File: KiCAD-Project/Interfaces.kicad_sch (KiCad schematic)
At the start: 56 parts, among them J201 XT30, J202 Conn_02x04_Odd_Even, J203 Conn_01x03_Shielded, J204 Conn_01x03_Shielded, U201 TI_TCAN337G, U202 TLE5012B_E1000, U203 MAX15062A

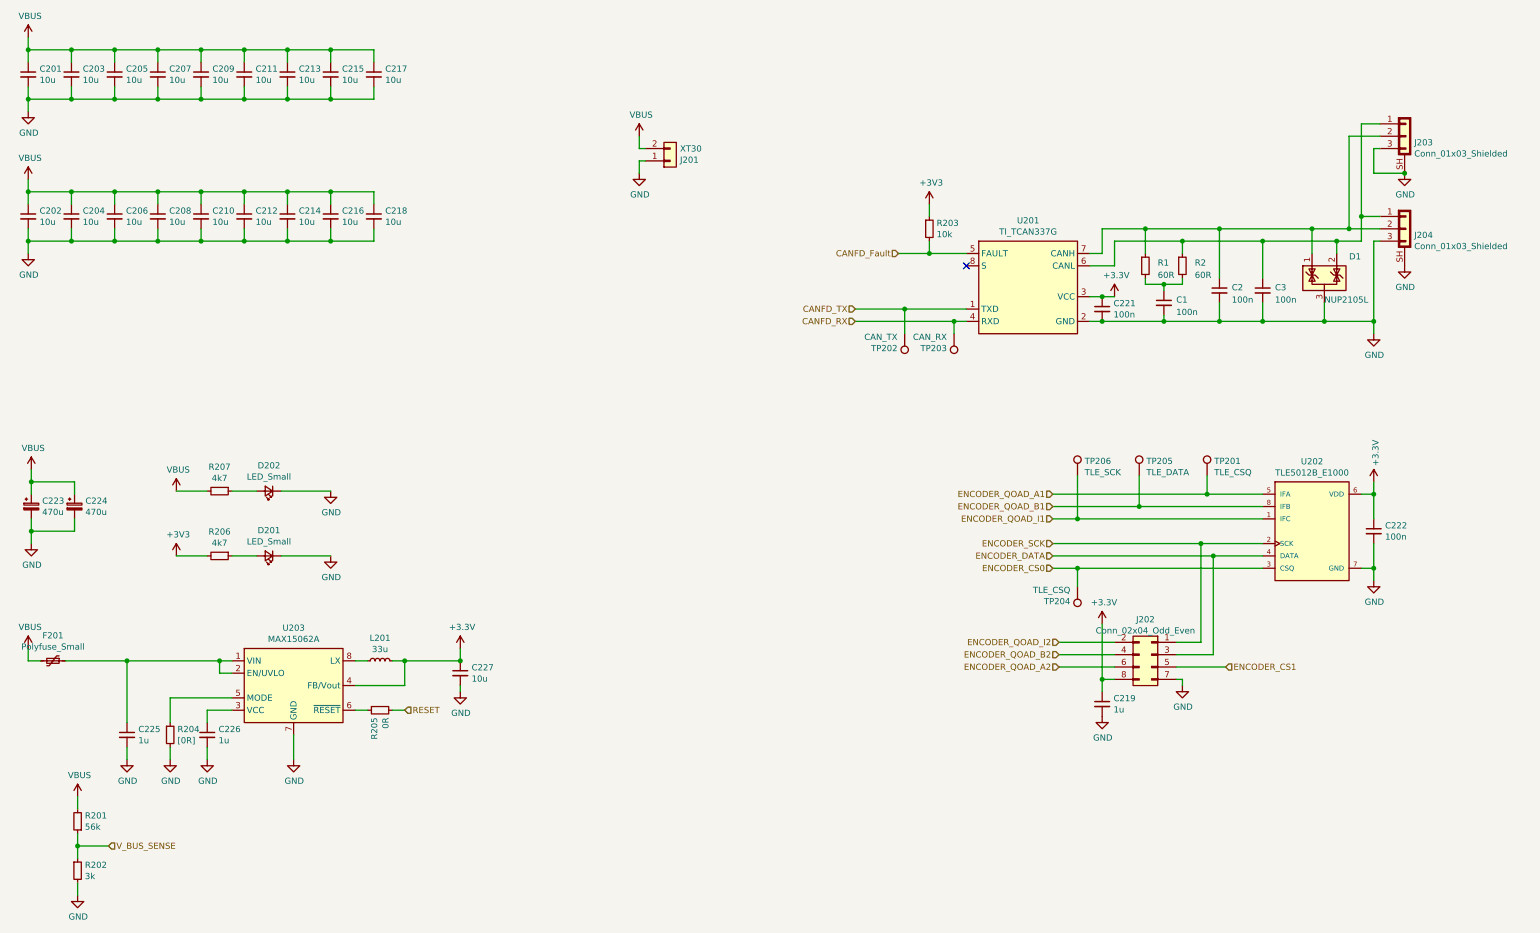
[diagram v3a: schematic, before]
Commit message: changed connectors to THT
changed connectors to THT, removed UART connector
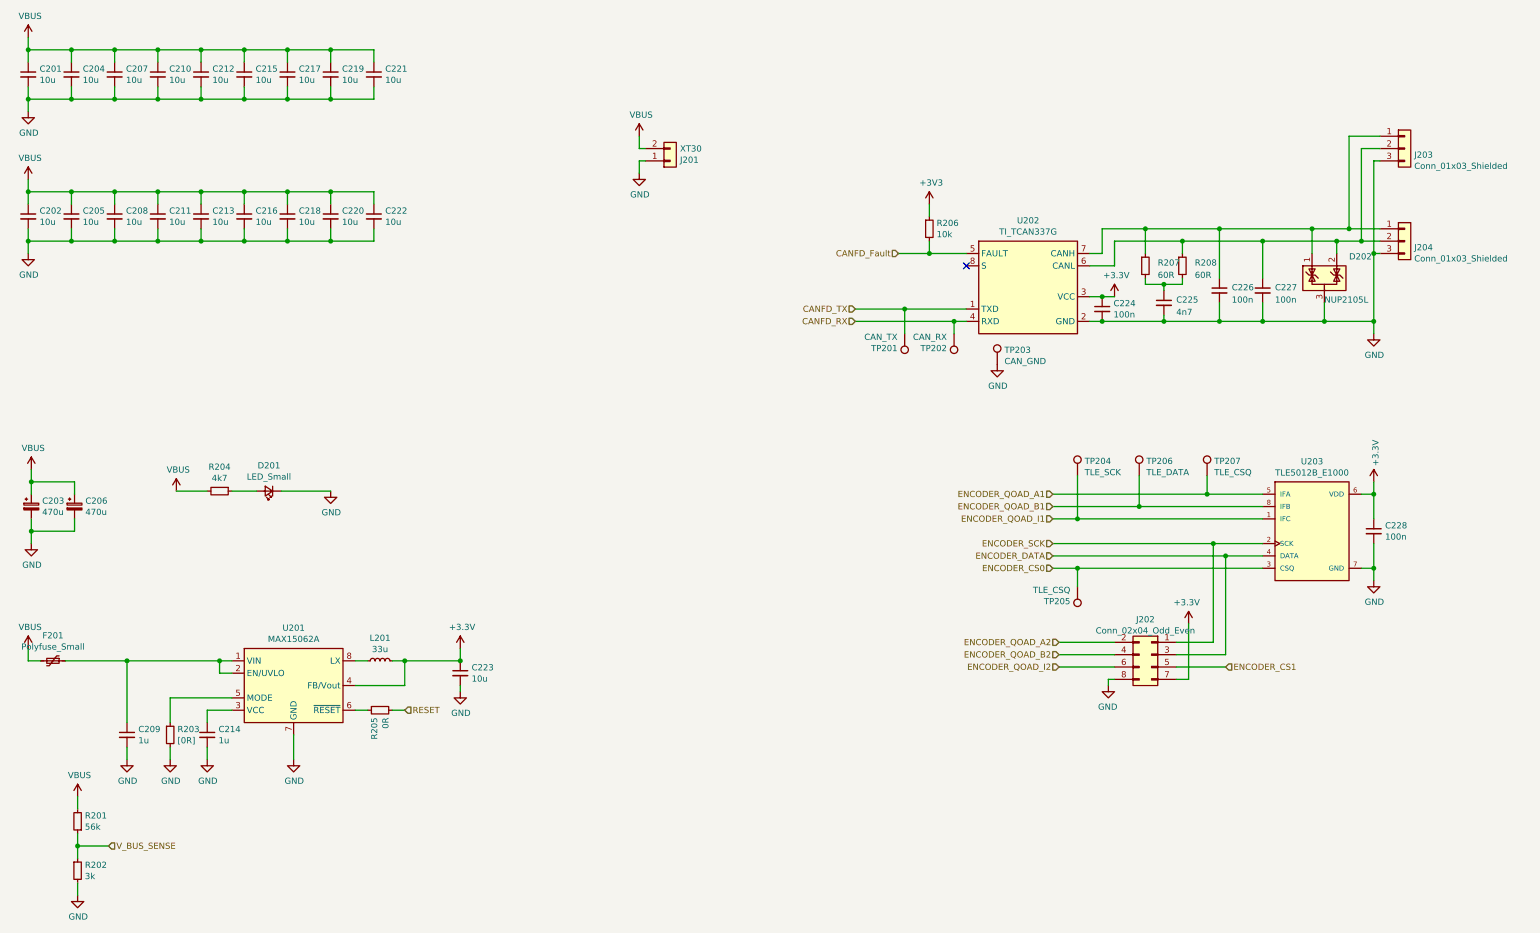
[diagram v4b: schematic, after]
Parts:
- removed C219: 1u, Capacitor_SMD:C_0603_1608Metric, symbol Device:C_Small
- removed D201: LED_Small, LED_SMD:LED_0603_1608Metric, symbol Device:LED_Small
- removed R206: 4k7, Resistor_SMD:R_0603_1608Metric, symbol Device:R_Small
- added TP203: CAN_GND, TestPoint:TestPoint_Pad_D1.5mm, symbol Connector:TestPoint
- C225: renamed from C1; value 100n -> 4n7
- J202: footprint Connector_PinHeader_2.54mm:PinHeader_2x04_P2.54mm_Vertical_SMD -> Connector_PinHeader_2.54mm:PinHeader_2x04_P2.54mm_Vertical
- J203, J204: footprint Connector_JST:JST_PH_S3B-PH-SM4-TB_1x03-1MP_P2.00mm_Horizontal -> Connector_JST:JST_PH_S3B-PH-K_1x03_P2.00mm_Horizontal; symbol Connector_Generic_Shielded:Conn_01x03_Shielded -> Connector_Generic:Conn_01x03
- renumbered C223 to C203, C203 to C204, C204 to C205, C224 to C206, C205 to C207, C206 to C208, C225 to C209, C207 to C210, C208 to C211, C209 to C212, C210 to C213, C226 to C214, C211 to C215, C212 to C216, C213 to C217, C214 to C218, C215 to C219, C216 to C220, C217 to C221, C218 to C222, C227 to C223, C221 to C224, C2 to C226, C3 to C227, C222 to C228, D202 to D201, D1 to D202, R204 to R203, R207 to R204, R203 to R206, R1 to R207, R2 to R208, TP202 to TP201, TP203 to TP202, TP206 to TP204, TP204 to TP205, TP205 to TP206, TP201 to TP207, U203 to U201, U201 to U202, U202 to U203
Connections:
- net +3V3: now also J202.7 (Pin_7); no longer J202.8 (Pin_8)
- net ENCODER_QOAD_A2: now also J202.2 (Pin_2); no longer J202.6 (Pin_6)
- net ENCODER_QOAD_I2: now also J202.6 (Pin_6); no longer J202.2 (Pin_2)
- net GND: now also J202.8 (Pin_8), TP203.1; no longer J202.7 (Pin_7), J203.SH (Shield), J204.SH (Shield)
- net at C227.1, D202.2 (K), R208.1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: now also J203.2 (Pin_2), J204.2 (Pin_2); no longer J203.1 (Pin_1), J204.1 (Pin_1)
- net at C226.1, D202.1 (K), R207.1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: now also J203.1 (Pin_1), J204.1 (Pin_1); no longer J203.2 (Pin_2), J204.2 (Pin_2)

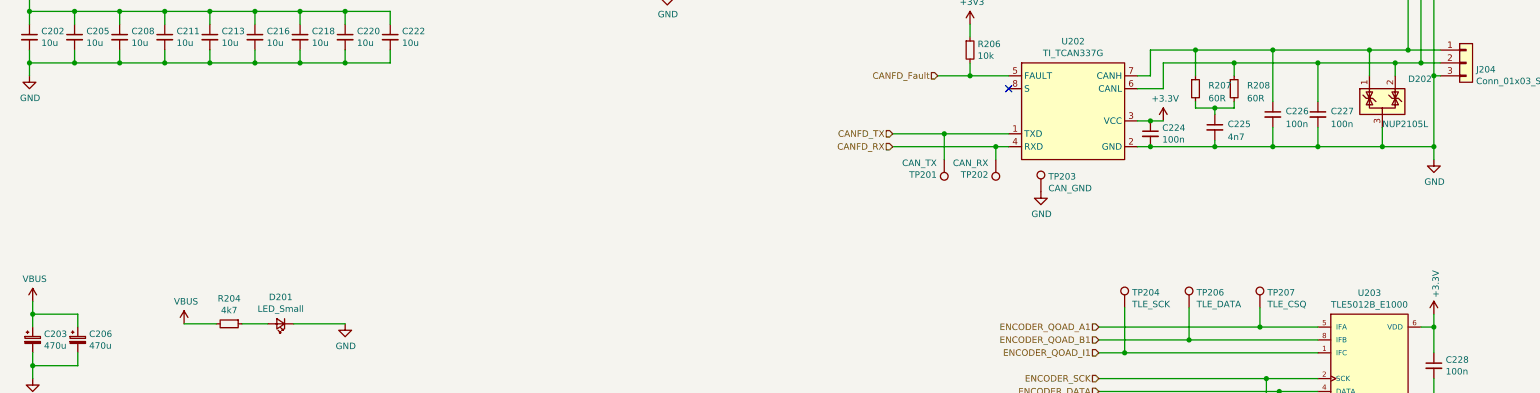
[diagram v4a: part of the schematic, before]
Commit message: minor pcb updates
swapped Encoder Quadrature signals, to provide debug UART
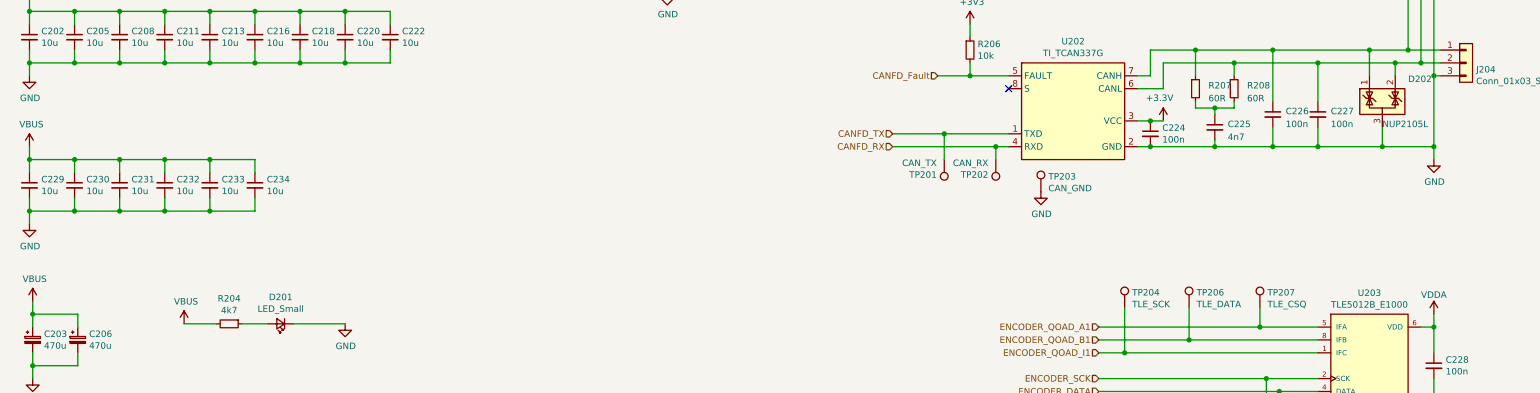
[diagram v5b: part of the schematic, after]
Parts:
- added C229, C230, C231, C232, C233, C234: 10u, Capacitor_SMD:C_1206_3216Metric, symbol Device:C_Small
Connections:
- net +3V3: no longer C228.1, U203.6 (VDD)
- net GND: now also C229.2, C230.2, C231.2, C232.2, C233.2, C234.2
- net VBUS: now also C229.1, C230.1, C231.1, C232.1, C233.1, C234.1
- new net VDDA: C228.1, U203.6 (VDD)
